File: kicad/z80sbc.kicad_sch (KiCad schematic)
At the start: 8 parts, among them J1 Conn_01x05_Female, U1 Z80CPU, U2 74HC00, U3 HM62256BLP, U4 MCP23017_SP, U5 AT28C256, U6 ATmega4809-P

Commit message: Schematic as built :-)
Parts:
- added RV1: 10K, symbol Device:R_Potentiometer
- added U7: 74HC00, symbol 74xx:74HC00
- added U8: LCD, Display:NHD-0420H1Z, symbol Display_Character:NHD-0420H1Z
- added U9: 74HC138, Package_DIP:DIP-16_W7.62mm, symbol NigelAtkinson:74HC138
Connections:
- net +5V: now also RV1.1, U7.14 (VCC), U8.16 (K), U8.2 (VDD), U9.16 (VCC)
- net A1: now also U8.4 (RS)
- net A15: now also U2.4; no longer U2.5
- net A4: now also U9.1 (A0)
- net A5: now also U9.2 (A1)
- net A6: now also U9.3 (A2)
- net A7: now also U9.4 (~{E1})
- net D0: now also U8.7 (DB0)
- net D1: now also U8.8 (DB1)
- net D2: now also U8.9 (DB2)
- net D3: now also U8.10 (DB3)
- net D4: now also U8.11 (DB4)
- net D5: now also U8.12 (DB5)
- net D6: now also U8.13 (DB6)
- net D7: now also U8.14 (DB7)
- net GND: now also RV1.3, U7.7 (GND), U8.1 (VSS), U8.15 (A), U9.8 (GND)
- net ~{IORQ}: now also U9.5 (~{E2}); no longer U6.4 (PC3)
- net ~{M1}: now also U9.6 (E3)
- net ~{RD}: now also U7.12, U7.13
- net at U2.12, U2.3: now also U2.5; no longer U2.4
- new net: RV1.2, U8.3 (VO)
- new net RD: U7.11, U8.5 (R/W)
- new net ~{LCD_IORQ}: U8.6 (E), U9.9 (~{Y6})
- new net ~{MCU_IORQ}: U6.4 (PC3), U9.7 (~{Y7})
- no-connect marks 15 -> 30
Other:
- title: Z80 SBC -> Z80 Bread board Computer
- moved on the sheet: U2A, U2B, U2C, U2D

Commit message: PCB Work in progress
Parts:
- removed U8: LCD, Display:NHD-0420H1Z, symbol Display_Character:NHD-0420H1Z
- added J2: Expansion Socket, Connector_PinSocket_2.54mm:PinSocket_2x20_P2.54mm_Vertical, symbol Connector_Generic:Conn_02x20_Counter_Clockwise
- added J3: LCD Socket, Connector_PinSocket_2.54mm:PinSocket_1x16_P2.54mm_Vertical, symbol Connector:Conn_01x16_Female
- added J4: IORQ Socket, Connector_PinSocket_2.54mm:PinSocket_1x06_P2.54mm_Vertical, symbol Connector:Conn_01x06_Female
- added R2, R3, R4: 10K, Resistor_THT:R_Axial_DIN0207_L6.3mm_D2.5mm_P10.16mm_Horizontal, symbol Device:R
- added SW1, SW2, SW3: SW_SPST, Button_Switch_THT:SW_PUSH_6mm, symbol Switch:SW_SPST
- J1: value Conn_01x05_Female -> Programming Socket; footprint (none) -> Connector_PinSocket_2.54mm:PinSocket_1x05_P2.54mm_Vertical
- R1: footprint (none) -> Resistor_THT:R_Axial_DIN0207_L6.3mm_D2.5mm_P10.16mm_Horizontal
- RV1: footprint (none) -> Potentiometer_THT:Potentiometer_Bourns_3386P_Vertical
- U1: footprint (none) -> Package_DIP:DIP-40_W15.24mm
- U2, U7: footprint (none) -> Package_DIP:DIP-14_W7.62mm
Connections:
- net +5V: now also J2.21 (Pin_21), J3.1 (Pin_1), J3.15 (Pin_15), R2.1, R3.1, R4.1; no longer U1.16 (~{INT}), U1.17 (~{NMI}), U1.24 (~{WAIT})
- net A0: now also J2.22 (Pin_22)
- net A1: now also J2.20 (Pin_20), J3.13 (Pin_13)
- net A10: now also J2.2 (Pin_2)
- net A11: now also J2.1 (Pin_1)
- net A12: now also J2.3 (Pin_3)
- net A13: now also J2.5 (Pin_5)
- net A14: now also J2.7 (Pin_7)
- net A15: now also J2.9 (Pin_9)
- net A2: now also J2.18 (Pin_18)
- net A3: now also J2.16 (Pin_16)
- net A4: now also J2.14 (Pin_14)
- net A5: now also J2.12 (Pin_12)
- net A6: now also J2.10 (Pin_10)
- net A7: now also J2.8 (Pin_8)
- net A8: now also J2.6 (Pin_6)
- net A9: now also J2.4 (Pin_4)
- net CLK: now also J2.11 (Pin_11)
- net D0: now also J2.27 (Pin_27), J3.10 (Pin_10)
- net D1: now also J2.29 (Pin_29), J3.9 (Pin_9)
- net D2: now also J2.23 (Pin_23), J3.8 (Pin_8)
- net D3: now also J2.15 (Pin_15), J3.7 (Pin_7)
- net D4: now also J2.13 (Pin_13), J3.6 (Pin_6)
- net D5: now also J2.17 (Pin_17), J3.5 (Pin_5)
- net D6: now also J2.19 (Pin_19), J3.4 (Pin_4)
- net D7: now also J2.25 (Pin_25), J3.3 (Pin_3)
- net GND: now also J2.24 (Pin_24), J3.16 (Pin_16), J3.2 (Pin_2), SW1.1 (A), SW2.2 (B), SW3.2 (B)
- net MODE: now also SW3.1 (A)
- net RD: now also J3.12 (Pin_12)
- net STEP: now also SW2.1 (A)
- net ~{BUSACK}: now also J2.36 (Pin_36)
- net ~{BUSRQ}: now also J2.32 (Pin_32)
- net ~{IORQ}: now also J2.39 (Pin_39)
- net ~{M1}: now also J2.28 (Pin_28)
- net ~{MREQ}: now also J2.37 (Pin_37)
- net ~{RD}: now also J2.40 (Pin_40)
- net ~{WR}: now also J2.38 (Pin_38)
- net at U9.10 (~{Y5}): now also J4.6 (Pin_6)
- net at U9.11 (~{Y4}): now also J4.5 (Pin_5)
- net at U9.12 (~{Y3}): now also J4.4 (Pin_4)
- net at U9.13 (~{Y2}): now also J4.3 (Pin_3)
- net at U9.14 (~{Y1}): now also J4.2 (Pin_2)
- net at U9.15 (~{Y0}): now also J4.1 (Pin_1)
- net VO: now reaches RV1.2
- net VO: now also J3.14 (Pin_14)
- net ~{HALT}: now reaches U1.18 (~{HALT})
- net ~{HALT}: now also J2.35 (Pin_35)
- net ~{RESET}: now reaches R1.2, U1.26 (~{RESET})
- net ~{RESET}: now also J2.30 (Pin_30), SW1.2 (B)
- net ~{RFSH}: now reaches U1.28 (~{RFSH})
- net ~{RFSH}: now also J2.26 (Pin_26)
- net ~{LCD_IORQ} renamed E
- net E: now also J3.11 (Pin_11)
- new net ~{INT}: J2.31 (Pin_31), R3.2, U1.16 (~{INT})
- new net ~{NMI}: J2.33 (Pin_33), R2.2, U1.17 (~{NMI})
- new net ~{WAIT}: J2.34 (Pin_34), R4.2, U1.24 (~{WAIT})
- no-connect marks 30 -> 22
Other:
- moved on the sheet: R1, RV1, U1, U7A, U7B, U7C, U7D

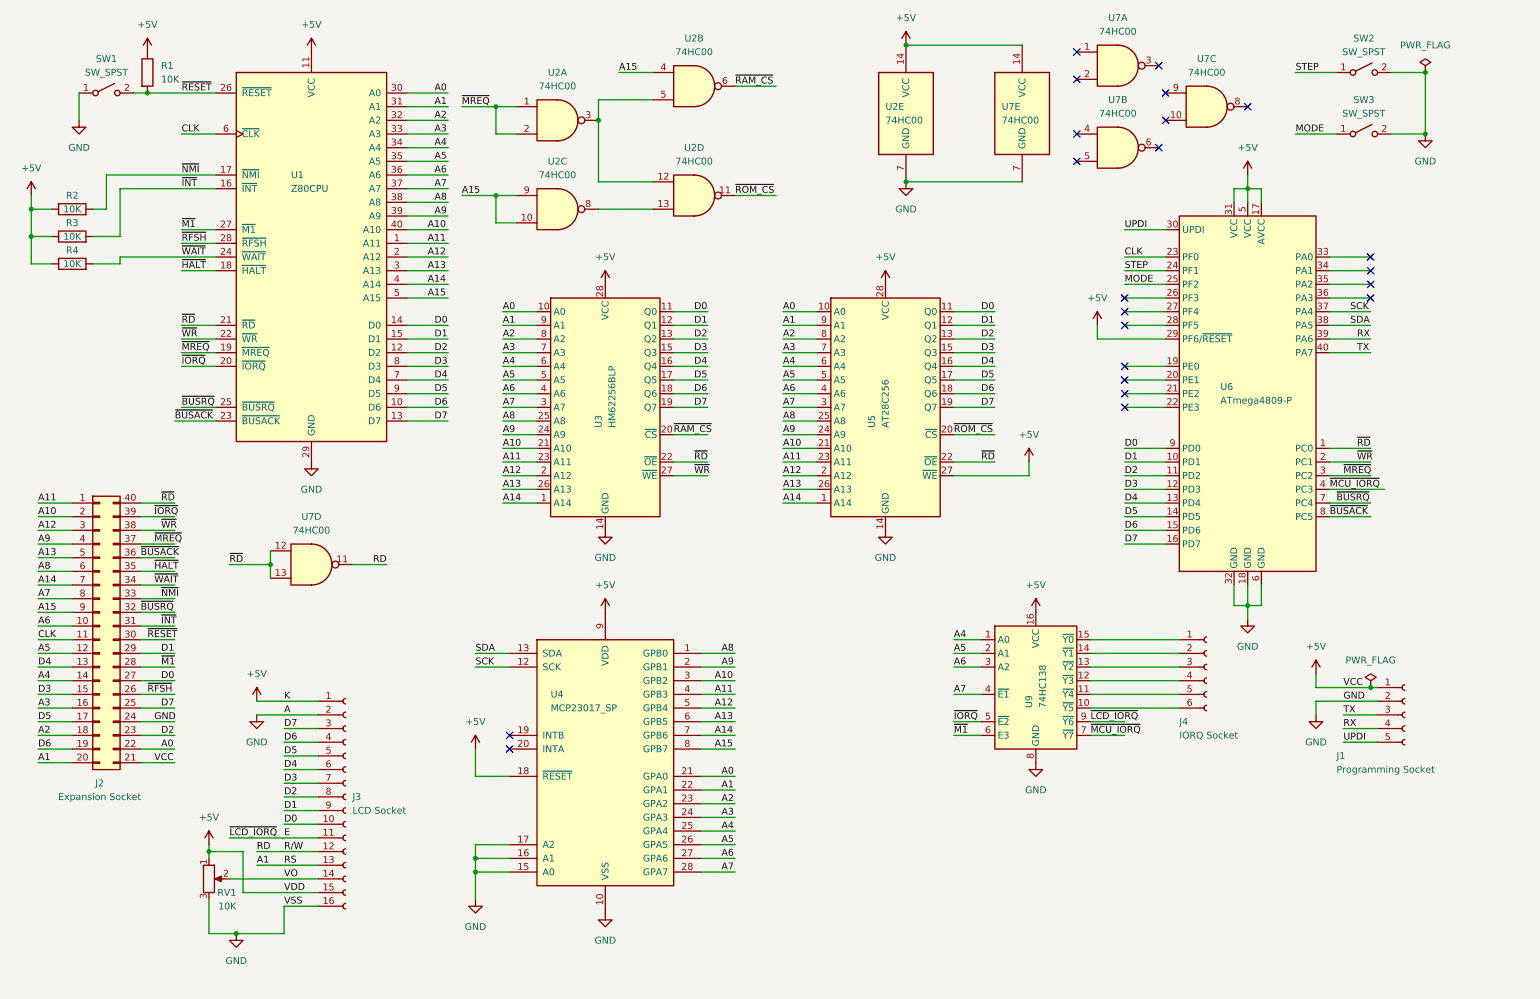
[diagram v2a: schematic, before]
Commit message: HW bugfix (lcd E line) and support RAM as fake ROM
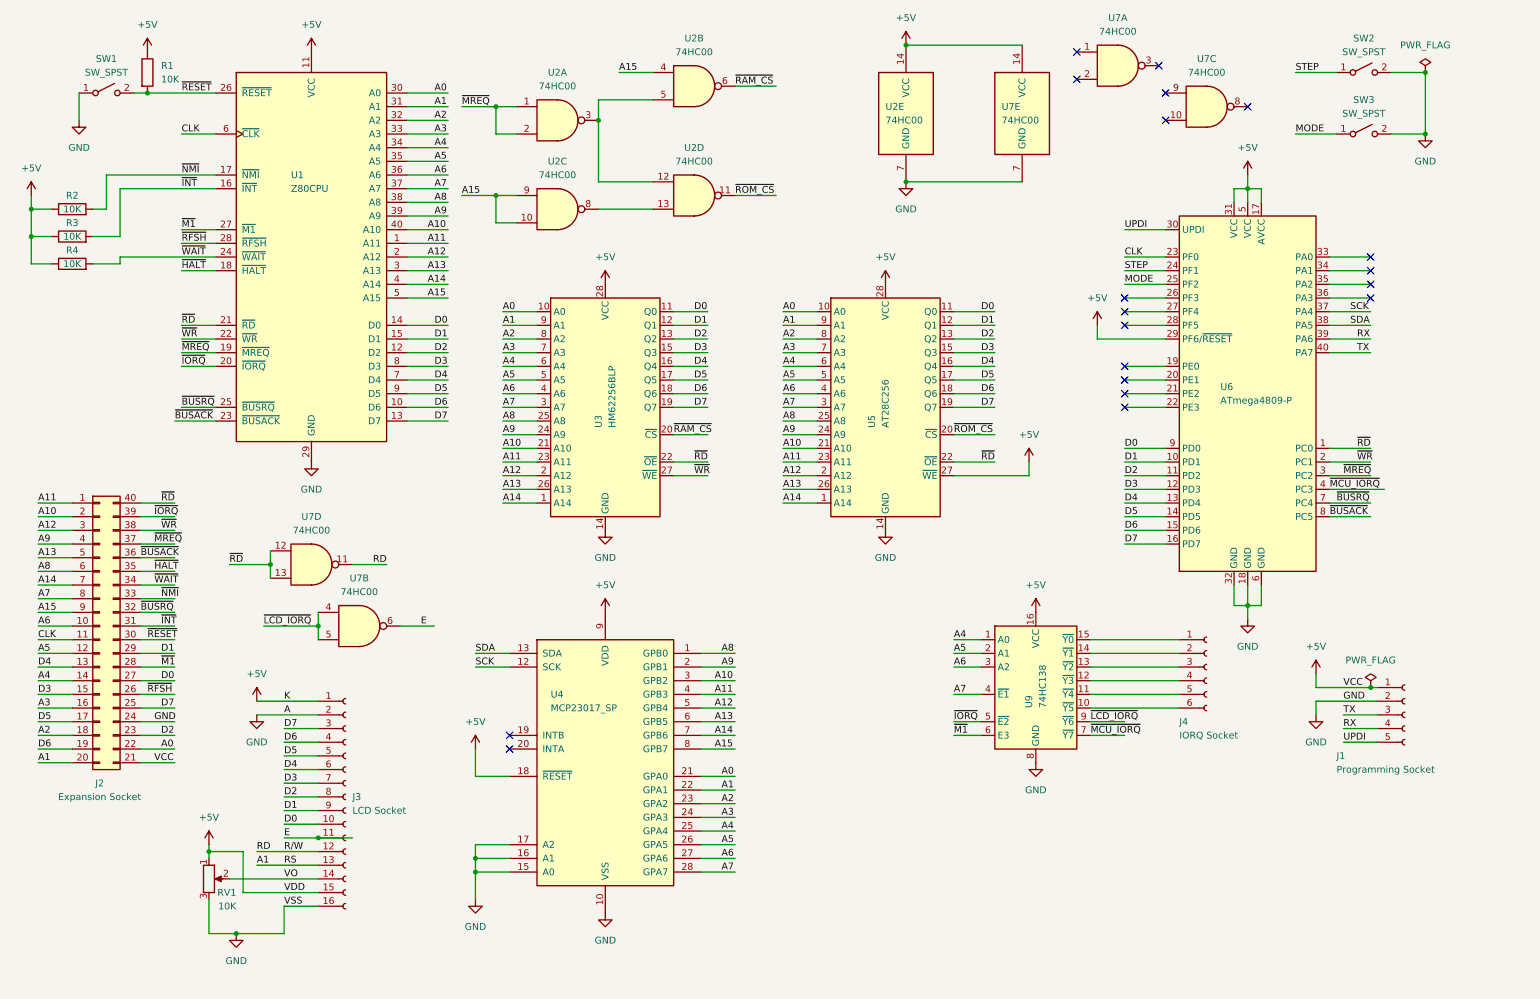
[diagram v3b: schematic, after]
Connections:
- net E: now also U7.6; no longer U9.9 (~{Y6})
- net ~{LCD_IORQ}: now reaches U7.4
- net ~{LCD_IORQ}: now also U7.5, U9.9 (~{Y6})
- no-connect marks 22 -> 19
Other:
- moved on the sheet: U7B
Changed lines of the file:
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@@
   (junction (at 243.84 48.26) (diameter 0) (color 0 0 0 0)
   )
+  (junction (at 71.12 168.91) (diameter 0) (color 0 0 0 0)
+  )
   (junction (at 180.34 21.59) (diameter 0) (color 0 0 0 0)
   )
@@
   )
   (junction (at 39.37 30.48) (diameter 0) (color 0 0 0 0)
+  )
+  (junction (at 71.12 129.54) (diameter 0) (color 0 0 0 0)
   )
   (junction (at 104.14 49.53) (diameter 0) (color 0 0 0 0)
@@
   (no_connect (at 212.09 27.94))
   (no_connect (at 227.33 25.4))
-  (no_connect (at 212.09 38.1))
   (no_connect (at 228.6 35.56))
-  (no_connect (at 227.33 40.64))
-  (no_connect (at 212.09 43.18))
   (no_connect (at 228.6 30.48))
   (no_connect (at 243.84 33.02))
@@
     (stroke (width 0) (type default) (color 0 0 0 0))
   )
+  (wire (pts (xy 71.12 168.91) (xy 77.47 168.91))
+    (stroke (width 0) (type default) (color 0 0 0 0))
+  )
   (wire (pts (xy 220.98 88.9) (xy 228.6 88.9))
     (stroke (width 0) (type default) (color 0 0 0 0))
@@
     (stroke (width 0) (type default) (color 0 0 0 0))
   )
+  (wire (pts (xy 71.12 127) (xy 71.12 129.54))
+    (stroke (width 0) (type default) (color 0 0 0 0))
+  )
   (wire (pts (xy 87.63 78.74) (xy 95.25 78.74))
     (stroke (width 0) (type default) (color 0 0 0 0))
@@
     (stroke (width 0) (type default) (color 0 0 0 0))
   )
+  (wire (pts (xy 71.12 129.54) (xy 71.12 132.08))
+    (stroke (width 0) (type default) (color 0 0 0 0))
+  )
   (wire (pts (xy 189.23 88.9) (xy 196.85 88.9))
     (stroke (width 0) (type default) (color 0 0 0 0))
@@
     (stroke (width 0) (type default) (color 0 0 0 0))
   )
+  (wire (pts (xy 86.36 129.54) (xy 92.71 129.54))
+    (stroke (width 0) (type default) (color 0 0 0 0))
+  )
   (wire (pts (xy 34.29 57.15) (xy 29.21 57.15))
     (stroke (width 0) (type default) (color 0 0 0 0))
@@
     (stroke (width 0) (type default) (color 0 0 0 0))
   )
+  (wire (pts (xy 60.96 129.54) (xy 71.12 129.54))
+    (stroke (width 0) (type default) (color 0 0 0 0))
+  )
   (wire (pts (xy 38.1 147.32) (xy 44.45 147.32))
     (stroke (width 0) (type default) (color 0 0 0 0))
@@
     (stroke (width 0) (type default) (color 0 0 0 0))
   )
-  (wire (pts (xy 54.61 168.91) (xy 71.12 168.91))
+  (wire (pts (xy 64.77 168.91) (xy 71.12 168.91))
     (stroke (width 0) (type default) (color 0 0 0 0))
   )
@@
     (effects (font (size 1.27 1.27)) (justify left bottom))
   )
+  (label "E" (at 90.17 129.54 0)
+    (effects (font (size 1.27 1.27)) (justify left bottom))
+  )
   (label "D7" (at 220.98 114.3 0)
     (effects (font (size 1.27 1.27)) (justify left bottom))
@@
     (effects (font (size 1.27 1.27)) (justify left bottom))
   )
-  (label "~{LCD_IORQ}" (at 54.61 168.91 0)
+  (label "~{LCD_IORQ}" (at 60.96 129.54 0)
     (effects (font (size 1.27 1.27)) (justify left bottom))
   )
@@
     (pin "1")
   )
-  (symbol (lib_id "74xx:74HC00") (at 219.71 40.64 0) (unit 2)
+  (symbol (lib_id "74xx:74HC00") (at 78.74 129.54 0) (unit 2)
     (in_bom yes) (on_board yes) (fields_autoplaced)
-    (property "Reference" "U7" (id 0) (at 219.71 31.75 0))
-    (property "Value" "74HC00" (id 1) (at 219.71 34.29 0))
-    (property "Footprint" "Package_DIP:DIP-14_W7.62mm" (id 2) (at 219.71 40.64 0)
-      (effects (font (size 1.27 1.27)) hide)
-    )
-    (property "Datasheet" "http://www.ti.com/lit/gpn/sn74hc00" (id 3) (at 219.71 40.64 0)
-      (effects (font (size 1.27 1.27)) hide)
-    )
+    (property "Reference" "U7" (id 0) (at 78.74 120.65 0))
+    (property "Value" "74HC00" (id 1) (at 78.74 123.19 0))
+    (property "Footprint" "Package_DIP:DIP-14_W7.62mm" (id 2) (at 78.74 129.54 0)
+      (effects (font (size 1.27 1.27)) hide)
+    )
+    (property "Datasheet" "http://www.ti.com/lit/gpn/sn74hc00" (id 3) (at 78.74 129.54 0)
+      (effects (font (size 1.27 1.27)) hide)
+    )
